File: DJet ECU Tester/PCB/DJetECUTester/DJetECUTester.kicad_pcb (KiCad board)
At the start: 2 copper layers, 162 x 90 mm, 152 parts, among them J1 ISP, J10 ECU3, J2 ECU1, J3 USB_B_Mini, J4 12V 4A IN (5.5/2.5), J5 12V IN, J6 MPS, J7 Conn_01x01, J8 Conn_01x01, J9 ECU2, Q1 MMBT2222ALT1G, Q10 MMBT2222ALT1G, Q11 MMBT2222ALT1G, Q12 MMBT2222ALT1G, Q2 MMBT2222ALT1G, Q3 MMBT2222ALT1G, Q4 MMBT2222ALT1G, Q5 MMBT2222ALT1G, Q6 MMBT2222ALT1G, Q7 MMBT2222ALT1G, Q8 MMBT2222ALT1G, Q9 MMBT2222ALT1G, U1 ATmega328P, U2 LM2596S-5, U3 FT232RL, U4 MCP41HV51-502E-ST, U5 MCP41HV51-502E-ST, U6 MCP23S08T-E_SO, U7 MCP41HV51-502E-ST, Y1 FA-238 16.0000MB-C3

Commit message: Completed layout. Added pull up resistors. Added ground stitching vias. Removed unused datasheets. Updated PDF schematic. Added manufacturing files. Added 3D model.
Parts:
- added R55: 1K, Resistor_SMD:R_0805_2012Metric, F.Cu at (250.8, 101.4)
- added R56: 100K, Resistor_SMD:R_0805_2012Metric, F.Cu at (253.0, 101.4)
- moved R44 22.2 mm to (183.6, 111.0)
- moved D8 21.9 mm to (179.5, 111.0)
- moved C18 15.9 mm to (242.6, 88.6), turned to 0 degrees
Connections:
- U6 pad 6: +5V -> Net-(R55-Pad2)
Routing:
- net +5V: track 226.2 -> 254.7 mm, vias 14 -> 15
- net /STATUS: track 3.65 -> 23.6 mm
- net Net-(R55-Pad2): track 0.00 -> 2.81 mm
- net /~IO_CS: track 60.8 -> 62.8 mm, vias 6 -> 4
- net /~RESET: track 32.1 -> 33.4 mm, vias 3 -> 2
- net /TPSWOT: track 53.0 -> 53.9 mm
- net GND: vias 186 -> 536

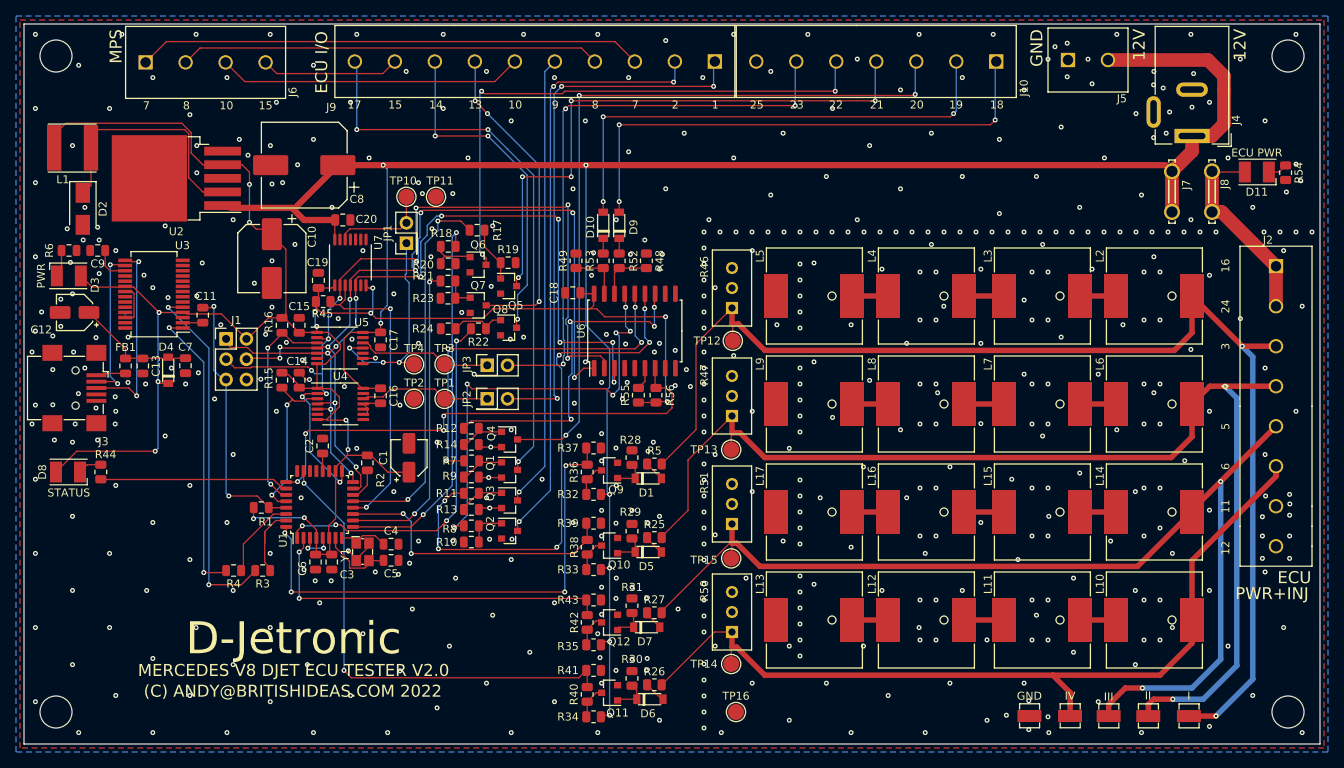
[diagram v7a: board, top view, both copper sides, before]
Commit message: Updated PCB to add resistor for fuel pump relay. Swapped trigger group signals 2 and 3 back to how they should be. Fuel pump now reports off when engine stopped.
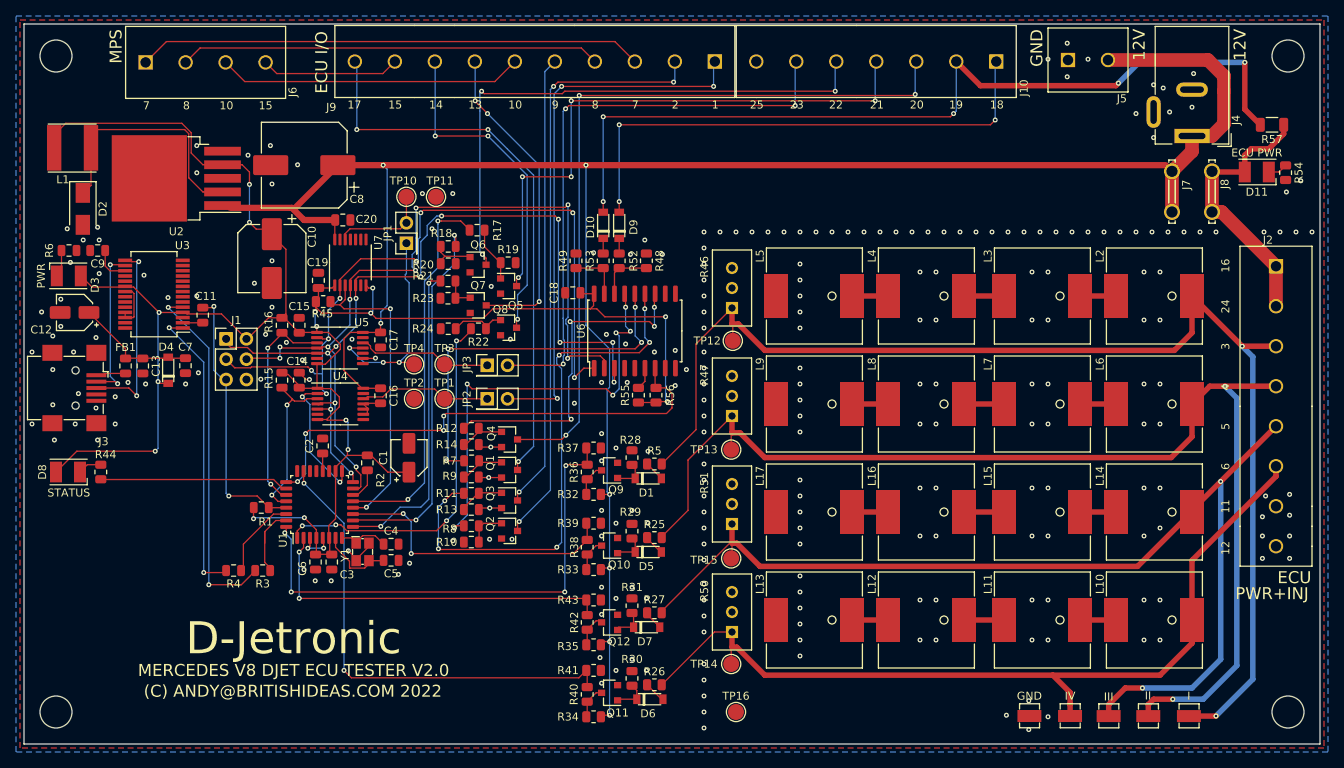
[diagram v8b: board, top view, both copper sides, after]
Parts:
- added R57: 680, Resistor_SMD:R_1206_3216Metric, F.Cu at (330.0, 67.6)
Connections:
- R18 pad 2: /TRIGGERGROUP2 -> /TRIGGERGROUP3
- R21 pad 2: /TRIGGERGROUP3 -> /TRIGGERGROUP2
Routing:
- net /ECU_FUELPUMPRELAY-19: track 62.5 -> 109.7 mm, vias 3 -> 5
- net /ECU_PWR: track 25.0 -> 34.2 mm
- net /TRIGGERGROUP2: track 47.9 -> 39.5 mm
- net /TRIGGERGROUP3: track 39.2 -> 47.0 mm
- net GND: vias 536 -> 256
